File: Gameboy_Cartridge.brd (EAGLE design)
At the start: 49.3 x 48 mm, 3 parts

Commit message: add mcu design
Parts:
- added U$2: STM32F405RG, gameboy:STM32F405RG
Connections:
- new net N$1: U$2.19, U$2.32, U$2.48, U$2.64
- new net N$2: U$2.18, U$2.63
- new net VBAT: U$2.1
- new net VDDA: U$2.13
- new net VSSA: U$2.12
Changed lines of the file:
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@@
 <?xml version="1.0" encoding="utf-8"?>
 <!DOCTYPE eagle SYSTEM "eagle.dtd">
-<eagle version="7.5.0">
+<eagle version="8.5.1">
 <drawing>
 <settings>
 <setting alwaysvectorfont="no"/>
+<setting keepoldvectorfont="yes"/>
 <setting verticaltext="up"/>
 </settings>
@@
 <param name="dpMaxLengthDifference" value="10mm"/>
 <param name="dpGapFactor" value="2.5"/>
-<param name="checkGrid" value="0"/>
 <param name="checkAngle" value="0"/>
 <param name="checkFont" value="1"/>
 <param name="checkRestrict" value="0"/>
+<param name="checkStop" value="0"/>
+<param name="checkValues" value="0"/>
 <param name="useDiameter" value="13"/>
 <param name="maxErrors" value="50"/>
@@
 <element name="R1" library="resistor" package="M0805" value="47K" x="39.98" y="41.58" rot="R180"/>
 <element name="C1" library="resistor" package="C0805" value="20nF" x="25.5" y="45"/>
+<element name="U$2" library="gameboy" package="STM32F405RG" value="STM32F405RG" x="14.8" y="29.7"/>
 </elements>
 <signals>
@@
 <wire x1="47.25" y1="4" x2="40.93" y2="41.58" width="0" layer="19" extent="1-1"/>
 </signal>
+<signal name="VDDA">
+<contactref element="U$2" pad="13"/>
+</signal>
+<signal name="VSSA">
+<contactref element="U$2" pad="12"/>
+</signal>
+<signal name="VBAT">
+<contactref element="U$2" pad="1"/>
+</signal>
+<signal name="N$1">
+<contactref element="U$2" pad="19"/>
+<contactref element="U$2" pad="64"/>
+<contactref element="U$2" pad="48"/>
+<contactref element="U$2" pad="32"/>
+<wire x1="11.05" y1="35.45" x2="9.05" y2="25.95" width="0" layer="19" extent="1-1"/>
+<wire x1="20.55" y1="33.45" x2="11.05" y2="35.45" width="0" layer="19" extent="1-1"/>
+<wire x1="20.55" y1="26.95" x2="20.55" y2="33.45" width="0" layer="19" extent="1-1"/>
+</signal>
+<signal name="N$2">
+<contactref element="U$2" pad="18"/>
+<contactref element="U$2" pad="63"/>
+<wire x1="20.55" y1="26.45" x2="9.05" y2="26.45" width="0" layer="19" extent="1-1"/>
+</signal>
 </signals>

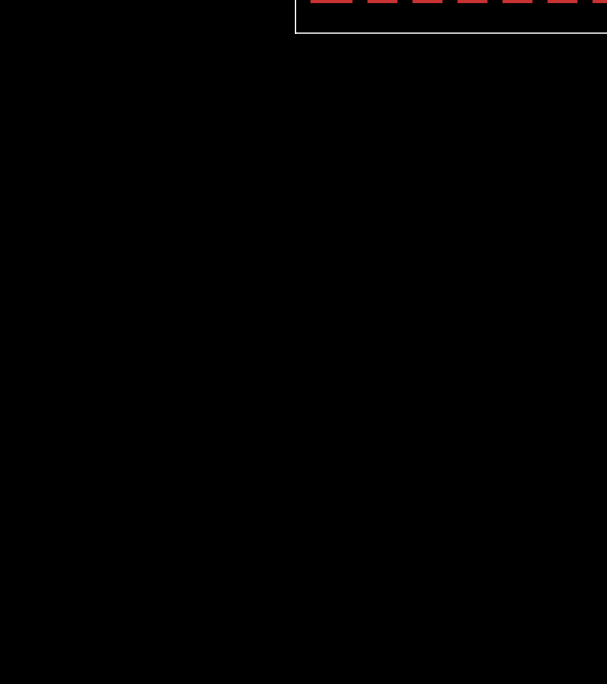
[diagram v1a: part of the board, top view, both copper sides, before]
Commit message: add programming header
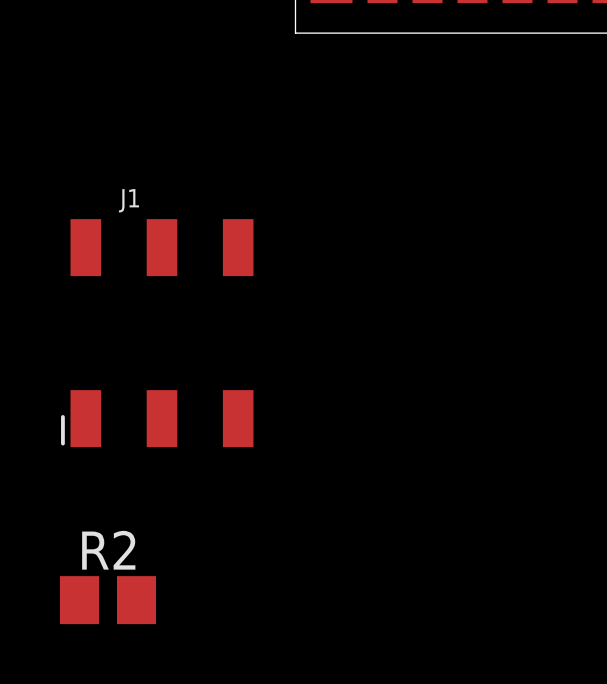
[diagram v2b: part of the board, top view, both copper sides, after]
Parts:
- added J1: (no value), SparkFun-Connectors:2X3_SMD
- added R2: 10K, resistor:M0805
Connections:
- new net N$3: J1.1, R2.2
- new net N$4: J1.3, R2.1
- new net N$5: J1.2, U$2.49
- new net N$7: J1.4, U$2.46
- new net N$8: J1.5, U$2.7
- new net N$9: J1.6, U$2.55

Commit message: connect mcu grounds
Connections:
- removed net VSSA: U$2.12
- net N$2: now also U$2.12
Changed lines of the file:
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@@
 <contactref element="U$2" pad="13"/>
-</signal>
-<signal name="VSSA">
-<contactref element="U$2" pad="12"/>
 </signal>
 <signal name="VBAT">
@@
 <contactref element="U$2" pad="18"/>
 <contactref element="U$2" pad="63"/>
-<wire x1="20.55" y1="26.45" x2="9.05" y2="26.45" width="0" layer="19" extent="1-1"/>
+<contactref element="U$2" pad="12"/>
+<wire x1="16.55" y1="23.95" x2="20.55" y2="26.45" width="0" layer="19" extent="1-1"/>
+<wire x1="9.05" y1="26.45" x2="16.55" y2="23.95" width="0" layer="19" extent="1-1"/>
 </signal>
 <signal name="N$3">

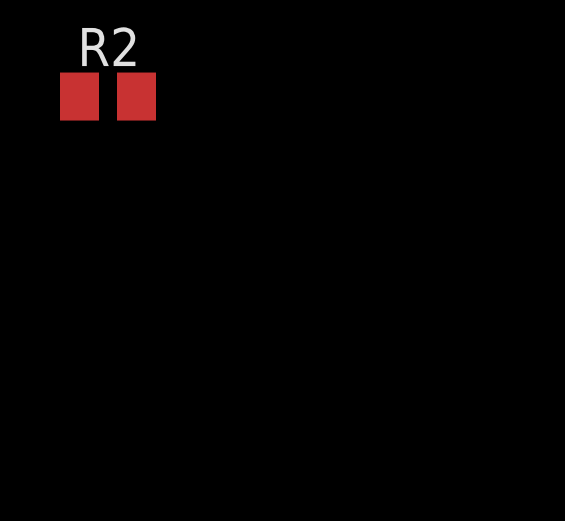
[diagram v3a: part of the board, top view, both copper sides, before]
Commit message: add VCAPs
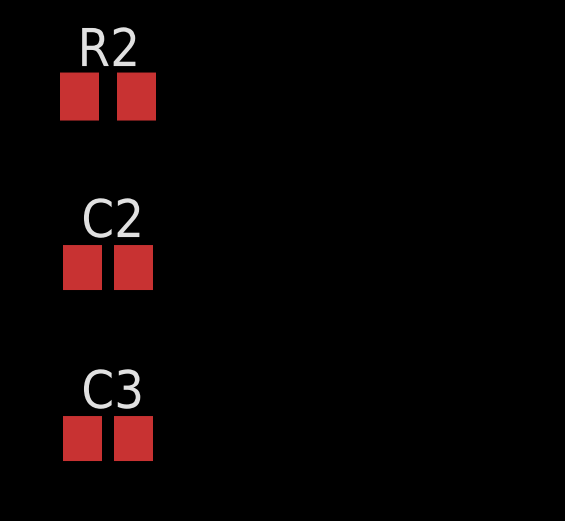
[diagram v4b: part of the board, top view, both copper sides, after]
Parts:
- added C2, C3: 2.2uF, resistor:C0805
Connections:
- new net N$10: C2.1, U$2.31
- new net N$11: C3.1, U$2.47
- new net N$12: C2.2, C3.2
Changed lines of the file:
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@@
 </element>
 <element name="R2" library="resistor" package="M0805" value="10K" x="-5.4" y="-18.9"/>
+<element name="C2" library="resistor" package="C0805" value="2.2uF" x="-5.4" y="-24.6"/>
+<element name="C3" library="resistor" package="C0805" value="2.2uF" x="-5.4" y="-30.3"/>
 </elements>
 <signals>
@@
 <wire x1="-1.06" y1="-7.15" x2="9.05" y2="30.45" width="0" layer="19" extent="1-1"/>
 </signal>
+<signal name="N$10">
+<contactref element="C2" pad="1"/>
+<contactref element="U$2" pad="31"/>
+<wire x1="-6.25" y1="-24.6" x2="20.55" y2="32.95" width="0" layer="19" extent="1-1"/>
+</signal>
+<signal name="N$11">
+<contactref element="U$2" pad="47"/>
+<contactref element="C3" pad="1"/>
+<wire x1="-6.25" y1="-30.3" x2="11.55" y2="35.45" width="0" layer="19" extent="1-1"/>
+</signal>
+<signal name="N$12">
+<contactref element="C3" pad="2"/>
+<contactref element="C2" pad="2"/>
+<wire x1="-4.55" y1="-24.6" x2="-4.55" y2="-30.3" width="0" layer="19" extent="1-1"/>
+</signal>
 </signals>

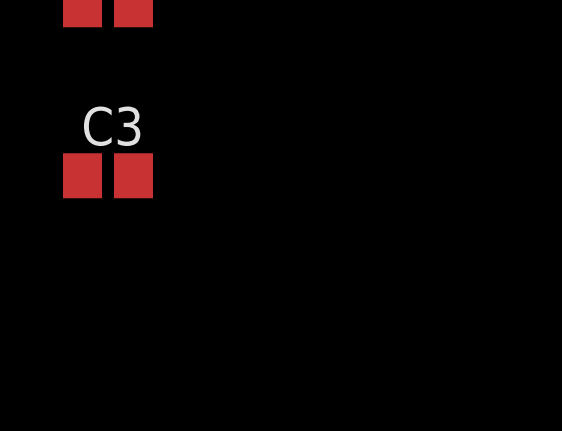
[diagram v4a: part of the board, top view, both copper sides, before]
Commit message: BOOT0 10k pullup
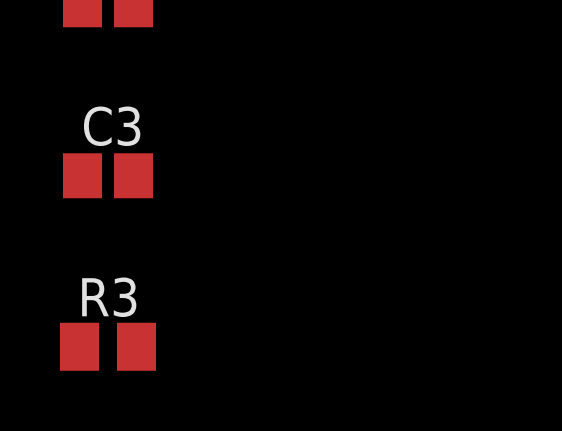
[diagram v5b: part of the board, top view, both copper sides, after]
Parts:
- added R3: 10K, resistor:M0805
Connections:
- new net N$6: R3.1, U$2.60
- net N$1: now also R3.2
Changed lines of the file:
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@@
 <element name="C2" library="resistor" package="C0805" value="2.2uF" x="-5.4" y="-24.6"/>
 <element name="C3" library="resistor" package="C0805" value="2.2uF" x="-5.4" y="-30.3"/>
+<element name="R3" library="resistor" package="M0805" value="10K" x="-5.4" y="-36"/>
 </elements>
 <signals>
@@
 <contactref element="U$2" pad="48"/>
 <contactref element="U$2" pad="32"/>
-<wire x1="11.05" y1="35.45" x2="9.05" y2="25.95" width="0" layer="19" extent="1-1"/>
-<wire x1="20.55" y1="33.45" x2="11.05" y2="35.45" width="0" layer="19" extent="1-1"/>
+<contactref element="R3" pad="2"/>
 <wire x1="20.55" y1="26.95" x2="20.55" y2="33.45" width="0" layer="19" extent="1-1"/>
+<wire x1="11.05" y1="35.45" x2="20.55" y2="33.45" width="0" layer="19" extent="1-1"/>
+<wire x1="9.05" y1="25.95" x2="11.05" y2="35.45" width="0" layer="19" extent="1-1"/>
+<wire x1="-4.45" y1="-36" x2="9.05" y2="25.95" width="0" layer="19" extent="1-1"/>
 </signal>
 <signal name="N$2">
@@
 <wire x1="-4.55" y1="-24.6" x2="-4.55" y2="-30.3" width="0" layer="19" extent="1-1"/>
 </signal>
+<signal name="N$6">
+<contactref element="U$2" pad="60"/>
+<contactref element="R3" pad="1"/>
+<wire x1="9.05" y1="27.95" x2="-6.35" y2="-36" width="0" layer="19" extent="1-1"/>
+</signal>
 </signals>

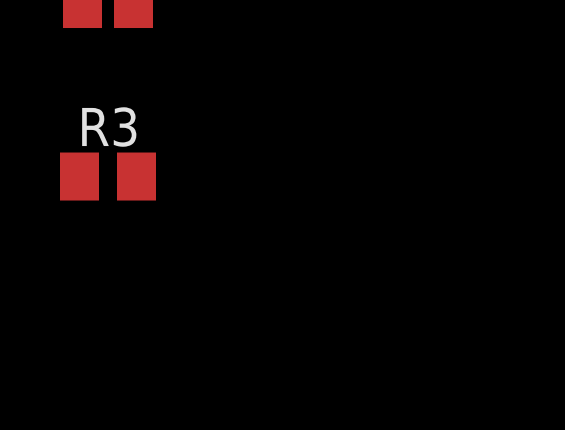
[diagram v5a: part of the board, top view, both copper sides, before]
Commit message: add cap on NRST
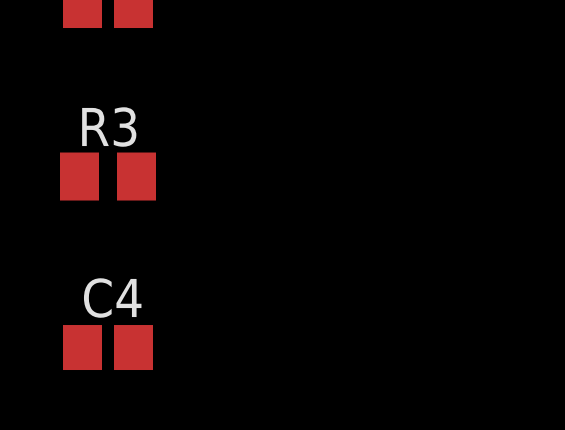
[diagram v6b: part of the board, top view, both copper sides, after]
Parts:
- added C4: 0.1uF, resistor:C0805
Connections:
- net N$4: now also C4.1
- net N$8: now also C4.2
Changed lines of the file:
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@@
 <element name="C3" library="resistor" package="C0805" value="2.2uF" x="-5.4" y="-30.3"/>
 <element name="R3" library="resistor" package="M0805" value="10K" x="-5.4" y="-36"/>
+<element name="C4" library="resistor" package="C0805" value="0.1uF" x="-5.4" y="-41.7"/>
 </elements>
 <signals>
@@
 <contactref element="R2" pad="1"/>
 <contactref element="J1" pad="3"/>
+<contactref element="C4" pad="1"/>
+<wire x1="-6.35" y1="-18.9" x2="-6.25" y2="-41.7" width="0" layer="19" extent="1-1"/>
 <wire x1="-3.6" y1="-12.85" x2="-6.35" y2="-18.9" width="0" layer="19" extent="1-1"/>
 </signal>
@@
 <contactref element="J1" pad="5"/>
 <contactref element="U$2" pad="7"/>
-<wire x1="-1.06" y1="-12.85" x2="14.05" y2="23.95" width="0" layer="19" extent="1-1"/>
+<contactref element="C4" pad="2"/>
+<wire x1="-1.06" y1="-12.85" x2="-4.55" y2="-41.7" width="0" layer="19" extent="1-1"/>
+<wire x1="14.05" y1="23.95" x2="-1.06" y2="-12.85" width="0" layer="19" extent="1-1"/>
 </signal>
 <signal name="N$9">
